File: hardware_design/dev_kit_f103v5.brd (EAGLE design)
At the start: 56.8 x 69.3 mm, 57 parts, among them J2 CON-SD-CARD_MICROSD-2908-05, U2 FT232RLSSOP, Y1 32.768kHz

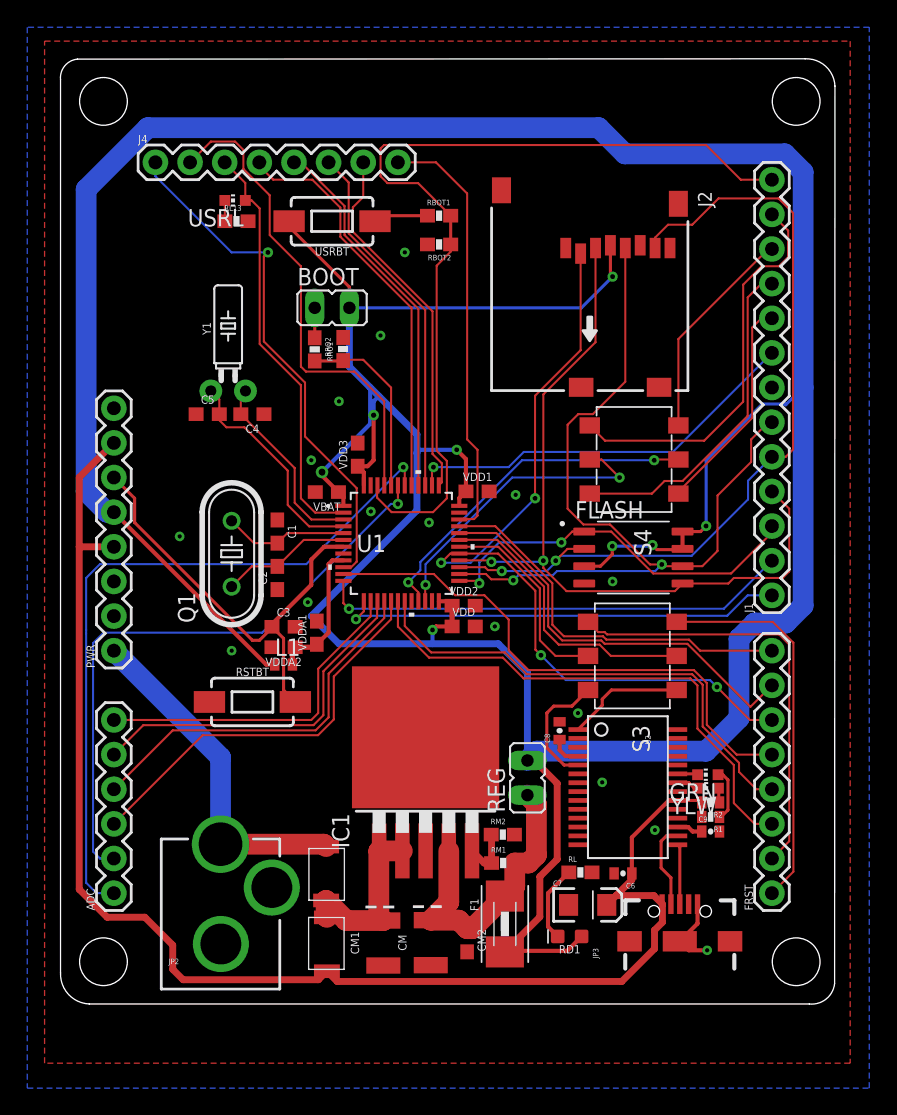
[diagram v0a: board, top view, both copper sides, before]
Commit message: Drill size was changed (20 mil)
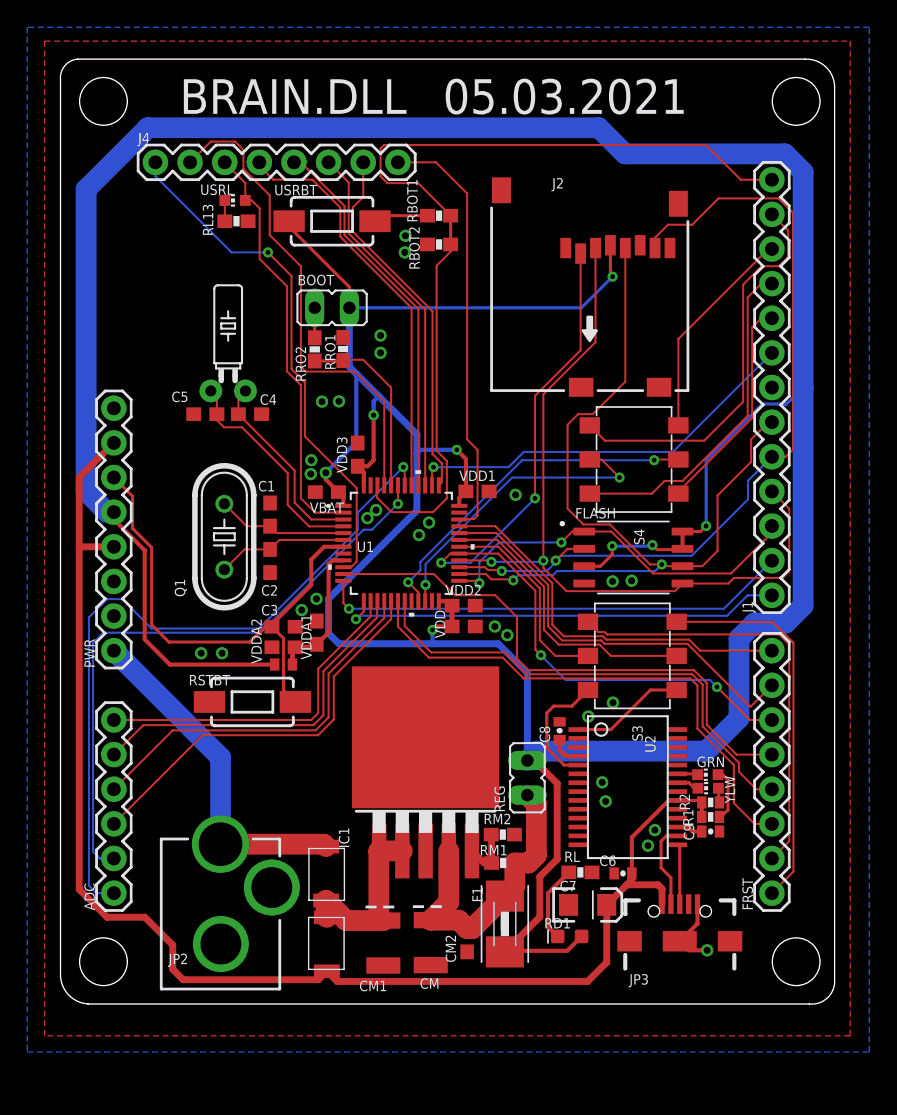
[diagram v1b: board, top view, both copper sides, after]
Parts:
- moved C1 1.35 mm to (25.4, 35.4)
- moved C2 1.35 mm to (25.4, 32.0)
- moved Q1 1.35 mm to (22.1, 33.8)
- moved C5 0.18 mm to (20.7, 42.7)
- moved C4 0.18 mm to (24.0, 42.7)
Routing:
- net NRST: track 33.1 -> 36.8 mm
- net 3.3V: track 319.9 -> 323.3 mm
- net V_USB: track 104.1 -> 101.1 mm
- net SCL1: track 52.7 -> 53.2 mm
- net GND: vias 16 -> 28
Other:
- outline, holes or cut-outs redrawn
- board text added: "05.03.2021"
- board text added: "BRAIN.DLL"

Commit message: Routes were be modified
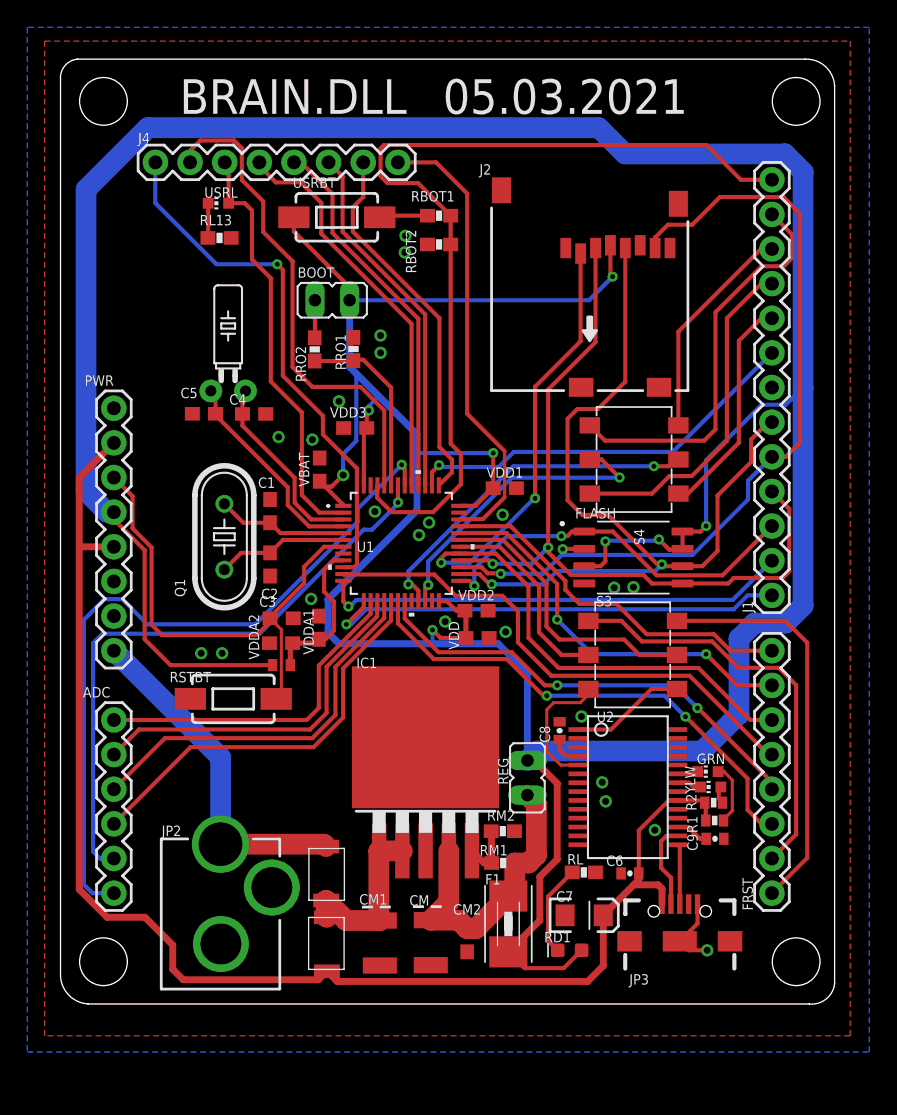
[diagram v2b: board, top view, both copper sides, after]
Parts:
- moved VDD1 2.01 mm to (42.6, 37.3)
- moved VDD3 1.96 mm to (31.7, 41.7), turned to 180 degrees
- moved RL13 1.74 mm to (21.7, 55.7)
- moved VBAT 1.73 mm to (29.1, 38.7), turned to 90 degrees
- moved RSTBT 1.42 mm to (22.7, 21.9)
- moved VDD 1.32 mm to (40.6, 26.3)
- moved USRL 1.24 mm to (21.6, 58.2)
- moved RD1 1.02 mm to (47.4, 3.43)
- moved VDD2 1.01 mm to (40.6, 28.3)
- moved C7 0.80 mm to (48.5, 5.99)
- moved RRO1 0.76 mm to (31.5, 47.5)
- moved C3 0.64 mm to (26.3, 27.8)
- moved C9 0.62 mm to (58.1, 11.6)
- moved BOOT 0.56 mm to (30.0, 51.1)
- moved C6 0.51 mm to (51.8, 9.07)
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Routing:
- net 3.3V: track 323.3 -> 330.9 mm
- net PB0: track 38.8 -> 36.5 mm, vias 0 -> 2
- net PA1: track 40.5 -> 38.2 mm
- net PB1: track 35.9 -> 33.7 mm, vias 0 -> 2
- net SWDIO: track 31.4 -> 33.4 mm
- net PA11: track 30.6 -> 29.1 mm, vias 0 -> 2
- net RX2: track 32.8 -> 34.3 mm
- net CRX1: track 28.2 -> 29.7 mm
- net PA12: track 28.5 -> 27.1 mm
- net PA0: track 38.1 -> 39.3 mm
- net N$35: track 5.62 -> 6.75 mm
- net VDDA: track 10.5 -> 11.5 mm
- net N$4: track 1.52 -> 2.55 mm
- net CTX1: track 31.7 -> 30.6 mm
- net MISO2: track 61.5 -> 62.5 mm
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
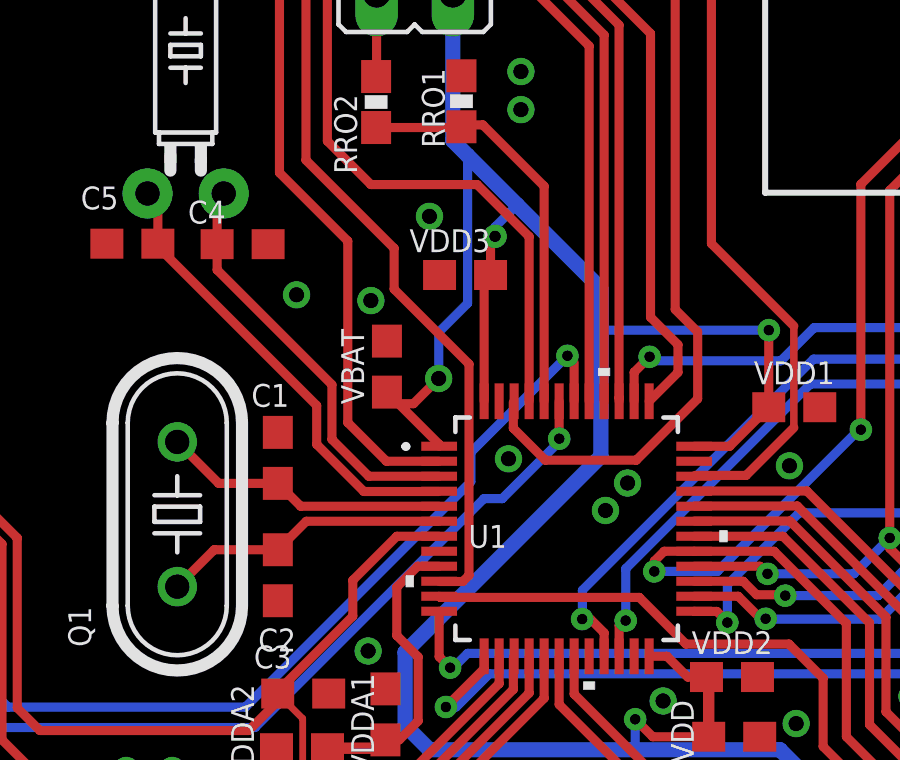
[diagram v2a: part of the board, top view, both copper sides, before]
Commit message: Bypass capacitors were located more close through to controller
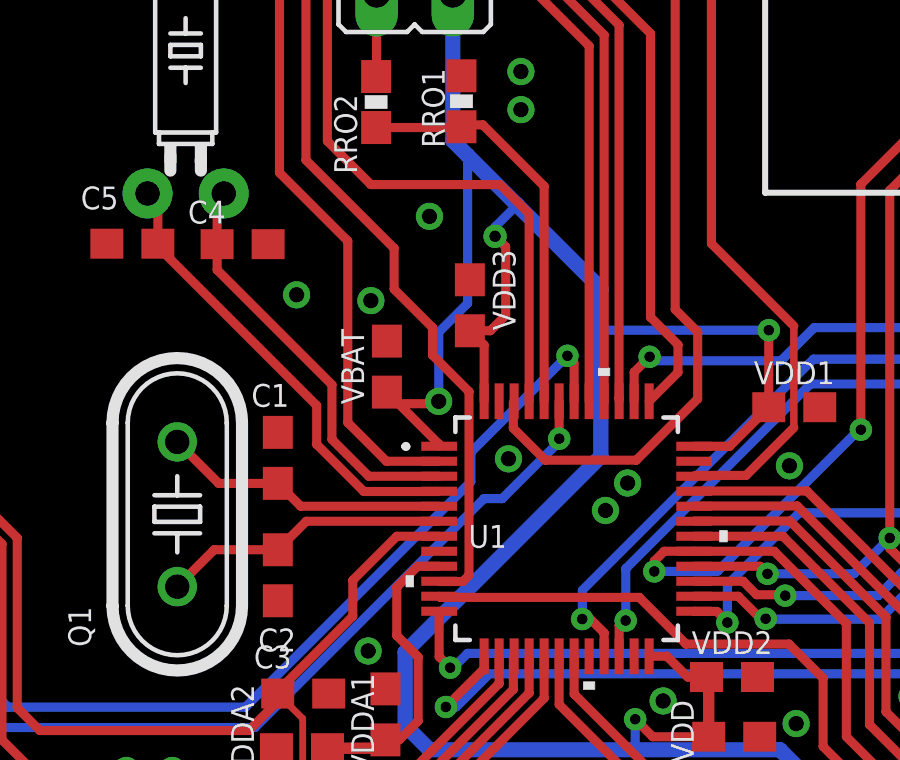
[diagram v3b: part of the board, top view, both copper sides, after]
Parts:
- moved VDD3 1.02 mm to (31.8, 40.7), turned to 90 degrees
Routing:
- net 3.3V: track 330.9 -> 332.5 mm
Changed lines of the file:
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@@
 <drawing>
 <settings>
-<setting alwaysvectorfont="yes"/>
+<setting alwaysvectorfont="no"/>
 <setting verticaltext="up"/>
 </settings>
@@
 <attribute name="VALUE" x="41.8846" y="27.848559375" size="0.762" layer="27" font="vector" ratio="15" align="top-center"/>
 </element>
-<element name="VDD3" library="SparkFun-Capacitors" library_urn="urn:adsk.eagle:library:510" package="0603" package3d_urn="urn:adsk.eagle:package:37414/1" value="100nF" x="31.666184375" y="41.7322" smashed="yes" rot="R180">
-<attribute name="NAME" x="31.158184375" y="43.2562" size="0.762" layer="25" font="vector" ratio="15" rot="R180" align="bottom-center"/>
-<attribute name="PROD_ID" value="CAP-00810" x="16.426184375" y="114.1222" size="1.778" layer="27" rot="R180" display="off"/>
-<attribute name="VALUE" x="31.666184375" y="40.2082" size="0.762" layer="27" font="vector" ratio="15" rot="R180" align="top-center"/>
+<element name="VDD3" library="SparkFun-Capacitors" library_urn="urn:adsk.eagle:library:510" package="0603" package3d_urn="urn:adsk.eagle:package:37414/1" value="100nF" x="31.8262" y="40.723815625" smashed="yes" rot="R90">
+<attribute name="NAME" x="33.3502" y="41.231815625" size="0.762" layer="25" font="vector" ratio="15" rot="R90" align="bottom-center"/>
+<attribute name="PROD_ID" value="CAP-00810" x="104.2162" y="55.963815625" size="1.778" layer="27" rot="R90" display="off"/>
+<attribute name="VALUE" x="30.3022" y="40.723815625" size="0.762" layer="27" font="vector" ratio="15" rot="R90" align="top-center"/>
 </element>
 <element name="VDDA1" library="SparkFun-Capacitors" library_urn="urn:adsk.eagle:library:510" package="0603" package3d_urn="urn:adsk.eagle:package:37414/1" value="1uF" x="29.011878125" y="27.086559375" smashed="yes" rot="R90">
@@
 <wire x1="31.75" y1="45.72" x2="31.75" y2="40.787071875" width="0.3048" layer="16"/>
 <wire x1="31.75" y1="40.787071875" x2="30.787340625" y2="39.8244125" width="0.3048" layer="16"/>
-<wire x1="30.787340625" y1="39.8244125" x2="30.787340625" y2="38.28263125" width="0.3048" layer="16"/>
-<via x="30.787340625" y="38.28263125" extent="1-16" drill="0.508"/>
-<wire x1="30.787340625" y1="38.28263125" x2="29.9466" y2="37.441890625" width="0.3048" layer="1"/>
-<wire x1="29.9466" y1="37.441890625" x2="29.449925" y2="37.441871875" width="0.3048" layer="1"/>
+<wire x1="30.787340625" y1="39.8244125" x2="30.787340625" y2="37.52063125" width="0.3048" layer="16"/>
+<via x="30.787340625" y="37.52063125" extent="1-16" drill="0.508"/>
+<wire x1="30.787340625" y1="37.52063125" x2="30.708628125" y2="37.44191875" width="0.3048" layer="1"/>
+<wire x1="30.708628125" y1="37.44191875" x2="29.449925" y2="37.441871875" width="0.3048" layer="1"/>
 <wire x1="29.062675" y1="37.829121875" x2="29.449925" y2="37.441871875" width="0.3048" layer="1"/>
 <wire x1="36.195" y1="39.878" x2="36.210240625" y2="39.893240625" width="0.3048" layer="16"/>
@@
 <wire x1="29.6672" y1="26.7208" x2="29.6672" y2="29.1592" width="0.508" layer="16"/>
 <wire x1="29.6672" y1="29.1592" x2="36.195" y2="35.687" width="0.508" layer="16"/>
-<wire x1="32.302" y1="41.518015625" x2="32.516184375" y2="41.7322" width="0.3048" layer="1"/>
-<wire x1="32.302" y1="37.524" x2="32.302" y2="41.518015625" width="0.3048" layer="1"/>
-<wire x1="32.516184375" y1="41.7322" x2="32.516184375" y2="42.871765625" width="0.3048" layer="1"/>
-<wire x1="32.516184375" y1="42.871765625" x2="32.6669375" y2="43.02251875" width="0.3048" layer="1"/>
+<wire x1="32.302" y1="37.524" x2="32.302" y2="39.398015625" width="0.3048" layer="1"/>
+<wire x1="32.302" y1="39.398015625" x2="31.8262" y2="39.873815625" width="0.3048" layer="1"/>
+<wire x1="32.6669375" y1="43.02251875" x2="33.02" y2="42.66945625" width="0.3048" layer="1"/>
+<wire x1="33.02" y1="42.66945625" x2="33.02" y2="40.386" width="0.3048" layer="1"/>
+<wire x1="33.02" y1="40.386" x2="32.507815625" y2="39.873815625" width="0.3048" layer="1"/>
+<wire x1="32.507815625" y1="39.873815625" x2="31.8262" y2="39.873815625" width="0.3048" layer="1"/>
 </signal>
 <signal name="VIN">
@@
 <wire x1="30.802" y1="31.524" x2="30.81" y2="31.516" width="0.1524" layer="1"/>
 <wire x1="31.592646875" y1="31.516" x2="30.81" y2="31.516" width="0.3048" layer="1"/>
-<wire x1="31.79768125" y1="38.764303125" x2="29.30144375" y2="41.260540625" width="0.3048" layer="1"/>
-<wire x1="31.79768125" y1="31.721034375" x2="31.79768125" y2="38.764303125" width="0.3048" layer="1"/>
+<wire x1="30.581990625" y1="39.97999375" x2="29.30144375" y2="41.260540625" width="0.3048" layer="1"/>
+<wire x1="31.79768125" y1="31.721034375" x2="31.79768125" y2="37.846" width="0.3048" layer="1"/>
 <wire x1="29.30144375" y1="41.260540625" x2="29.30144375" y2="42.6237375" width="0.3048" layer="1"/>
 <wire x1="29.30144375" y1="42.6237375" x2="26.362659375" y2="45.562521875" width="0.3048" layer="1"/>
@@
 <wire x1="17.018" y1="58.2168" x2="17.018" y2="61.214" width="0.3048" layer="16"/>
 <wire x1="21.49348125" y1="53.74131875" x2="17.018" y2="58.2168" width="0.3048" layer="16"/>
+<wire x1="31.79768125" y1="37.846" x2="30.581990625" y2="39.061690625" width="0.3048" layer="1"/>
+<wire x1="30.581990625" y1="39.061690625" x2="30.581990625" y2="39.97999375" width="0.3048" layer="1"/>
 </signal>
 <signal name="PA4">
@@
 <contactref element="U1" pad="45"/>
 <contactref element="J4" pad="2"/>
-<wire x1="33.802" y1="37.524" x2="33.802" y2="43.01268125" width="0.3048" layer="1"/>
-<wire x1="28.5264125" y1="44.74671875" x2="32.0679625" y2="44.74671875" width="0.3048" layer="1"/>
+<wire x1="33.802" y1="37.524" x2="33.802" y2="43.77468125" width="0.3048" layer="1"/>
+<wire x1="28.5264125" y1="44.74671875" x2="32.8299625" y2="44.74671875" width="0.3048" layer="1"/>
 <wire x1="23.352759375" y1="62.245240625" x2="22.783796875" y2="62.814203125" width="0.3048" layer="1"/>
 <wire x1="24.925021875" y1="58.350053125" x2="23.352759375" y2="59.922315625" width="0.3048" layer="1"/>
@@
 <wire x1="20.31238125" y1="62.814203125" x2="19.558" y2="62.059821875" width="0.3048" layer="1"/>
 <wire x1="19.558" y1="62.059821875" x2="19.558" y2="61.214" width="0.3048" layer="1"/>
-<wire x1="33.802" y1="43.01268125" x2="32.0679625" y2="44.74671875" width="0.3048" layer="1"/>
+<wire x1="33.802" y1="43.77468125" x2="32.8299625" y2="44.74671875" width="0.3048" layer="1"/>
 <wire x1="24.925021875" y1="58.350053125" x2="24.925021875" y2="56.106059375" width="0.3048" layer="1"/>
 <wire x1="24.925021875" y1="56.106059375" x2="27.0764" y2="53.95468125" width="0.3048" layer="1"/>
